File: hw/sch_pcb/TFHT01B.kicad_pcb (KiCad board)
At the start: 2 copper layers, 30 x 15 mm, 31 parts, among them J1 SM04B-GHS-TB, J2 SM04B-GHS-TB, M1 M3, M2 M3, M3 M3, M4 M3, M5 M3, M6 M3, M7 CAP-SF2, Q1 BC817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

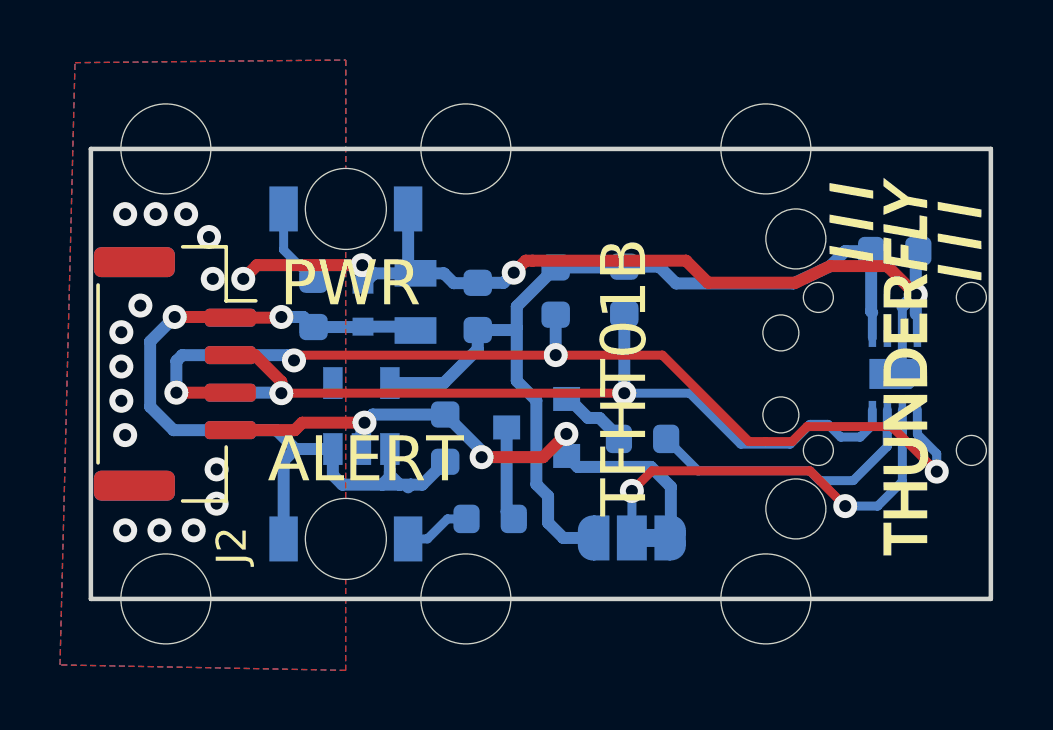
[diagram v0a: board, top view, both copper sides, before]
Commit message: Improve heat insulation of sensor #7.
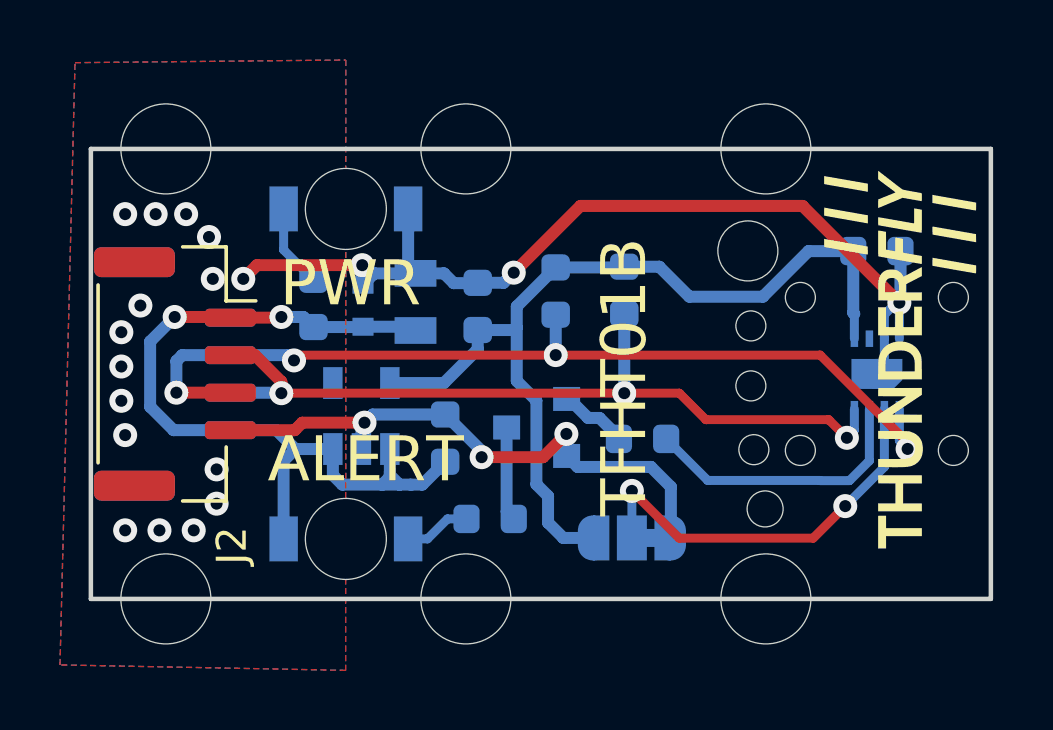
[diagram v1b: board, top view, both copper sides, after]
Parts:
- added H1: Heat insulation, MountingHole:MountingHole_2mm, F.Cu at (154.7, 115.2)
- moved REF** 1.65 mm to (154.5, 108.5)
- moved REF** 1.39 mm to (154.6, 113.0)
- moved REF** 1.03 mm to (154.6, 111.0)
- moved REF** 1.02 mm to (155.1, 117.1)
- moved M7 0.60 mm to (158.8, 112.6)
- moved U1 0.60 mm to (158.8, 112.6)
- moved C5 0.60 mm to (158.8, 108.5)
- moved G*** 0.29 mm to (159.6, 112.2)
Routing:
- net /SDA: track 34.1 -> 31.7 mm
- net /SCL: track 28.3 -> 27.3 mm, vias 2 -> 3
- net Net-(JP1-Pad2): track 14.1 -> 13.5 mm

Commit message: Kontrola a upravy pred vyrobou
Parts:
- removed REF** (x4): dira_2mm, Mlab_Mechanical:dira_2mm
- removed REF**: dira_0.4mm, Mlab_Mechanical:dira_0.4mm
- added H2: Heat insulation, MountingHole:MountingHole_2mm, F.Cu at (154.2, 108.5)
- added H3: Heat insulation, Mlab_Mechanical:MountingHole_1mm, F.Cu at (155.4, 117.2)
- added H4: Heat insulation, Mlab_Mechanical:MountingHole_1mm, F.Cu at (154.2, 113.1)
- added H5: Heat insulation, Mlab_Mechanical:MountingHole_1mm, F.Cu at (154.2, 111.0)
- D2, D3: footprint Mlab_D:LED_1206 -> Mlab_D:LED_1206_mill
- H1: footprint MountingHole:MountingHole_2mm -> Mlab_Mechanical:MountingHole_1mm
- moved H1 0.43 mm to (154.2, 115.2)
- moved J1 0.20 mm to (135.6, 112.6)
- moved J2 0.20 mm to (135.6, 112.6)
- turned R4 to 180 degrees
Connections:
- D3 pad 1: Net-(D3-Pad1) -> Net-(D3-K)
- D3 pad 2: +5V -> Net-(D3-A)
- Q1 pad 3: Net-(Q1-Pad3) -> Net-(D3-K)
- R4 pad 1: Net-(D3-Pad1) -> +5V
- R4 pad 2: Net-(Q1-Pad3) -> Net-(D3-A)
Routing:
- net Net-(D3-A): track 0.00 -> 7.92 mm, vias 0 -> 2
- net Net-(D3-K): track 0.00 -> 5.99 mm, vias 0 -> 2
- net Net-(Q1-Pad3): track 3.15 -> 0.00 mm
- net Net-(D3-Pad1): track 2.22 -> 0.00 mm
